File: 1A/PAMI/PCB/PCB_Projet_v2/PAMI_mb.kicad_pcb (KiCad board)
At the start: 4 copper layers, 65 x 56 mm, 106 parts, among them J101 Conn_02x20_Odd_Even, J103 Conn_ST_STDC14, J104 Battery, J105 Charge, J106 Stop, J107 Conn_01x04, J108 173010542, J110 Conn_01x04, J111 Conn_01x04, J112 Conn_01x04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

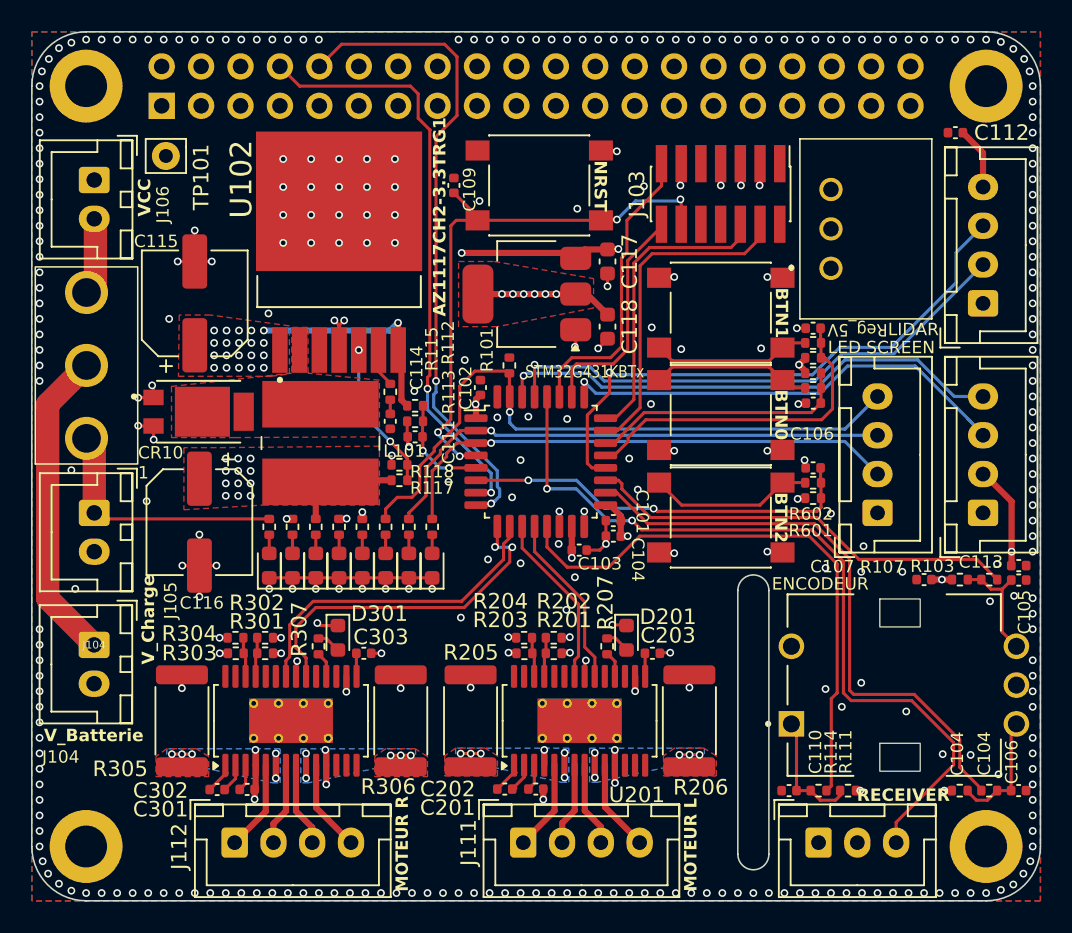
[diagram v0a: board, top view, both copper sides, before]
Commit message: add PAMI PCB Teardrops, export gerbers
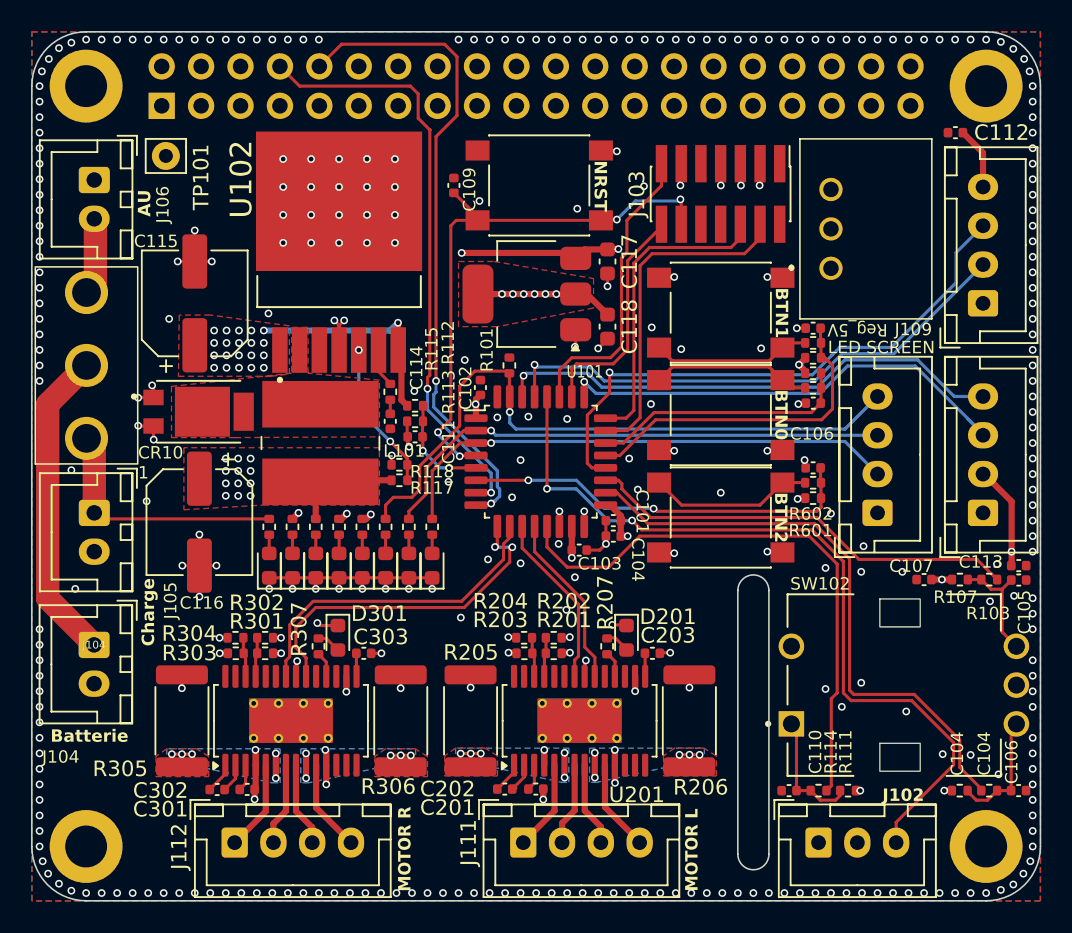
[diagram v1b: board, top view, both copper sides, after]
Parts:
- C201, C301: value 100nF -> 100n
- C202, C302: value 22nF -> 22n
- C203, C303: value 2.2uF -> 2u2
- renumbered RECEIVER to J102, LIDAR to J109, ENCODEUR to SW102, STM32G431KBTx to U101
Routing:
- net Net-(U301-CPO): track 2.67 -> 1.99 mm
- net GND: vias 326 -> 327
- added copper zone on F.Cu, net Net-(U201-BRA)
- added copper zone on F.Cu, net Net-(U201-BRB)
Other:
- board text added: "AU"
- board text added: "Batterie"
- board text added: "Charge"
- board text added: "MOTOR L"
- board text added: "MOTOR R"
- board text removed: "AZ1117CH2-3.3TRG1"
- board text removed: "MOTEUR L"
- board text removed: "MOTEUR R"
- board text removed: "VCC"
- board text removed: "V_Batterie"
- board text removed: "V_Charge"
